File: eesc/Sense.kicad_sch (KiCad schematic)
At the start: 0 parts

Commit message: Add current sense and finish DRV8301 Circuit
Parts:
- added C30, C32, C33: 100n, symbol Device:C
- added IC1, IC2, IC3: MC74VHC1GT66, SOT95P275X110-5N, symbol MC74VHC1GT66:MC74VHC1GT66
- added Q1: DMN62D0U, Package_TO_SOT_SMD_AKL:SOT-23, symbol PCM_Transistor_MOSFET_AKL:DMN62D0U
- added R10, R12, R7, R9: 2.2k, symbol Device:R
- added R11, R13, R6, R8: 39k, symbol Device:R
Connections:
- new net: C33.2, IC3.1 (IN/OUT_XA)
- new net: C30.2, IC1.1 (IN/OUT_XA)
- new net: C32.2, IC2.1 (IN/OUT_XA)
- new net: Q1.3 (D), R6.2
- new net +3.3V: IC1.5 (VCC), IC2.5 (VCC), IC3.5 (VCC)
- new net +5V: Q1.1 (G)
- new net GND: IC1.2 (OUT/IN_YA), IC1.3 (GND), IC2.2 (OUT/IN_YA), IC2.3 (GND), IC3.2 (OUT/IN_YA), IC3.3 (GND), R10.1, R12.1, R7.2, R9.1
- new net SENS_A: C30.1, R8.1, R9.2
- new net SENS_B: C32.1, R10.2, R11.1
- new net SENS_C: C33.1, R12.2, R13.1
- new net SENS_FILTERED: IC1.4 (ON/OFF_CONTROL), IC2.4 (ON/OFF_CONTROL), IC3.4 (ON/OFF_CONTROL)
- new net SENS_SUPPLY: Q1.2 (S), R7.1
- new net SH_A: R8.2
- new net SH_B: R11.2
- new net SH_C: R13.2
- new net V_SUPPLY: R6.1
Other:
- note added: "Current Sensing is implemented to figure out rotor position and apply proper signals to maximimze torque on motor"
- note added: "Current Sensor A"
- note added: "Current Sensor B"
- note added: "Current Sensor C"
- note added: "Power Sense"

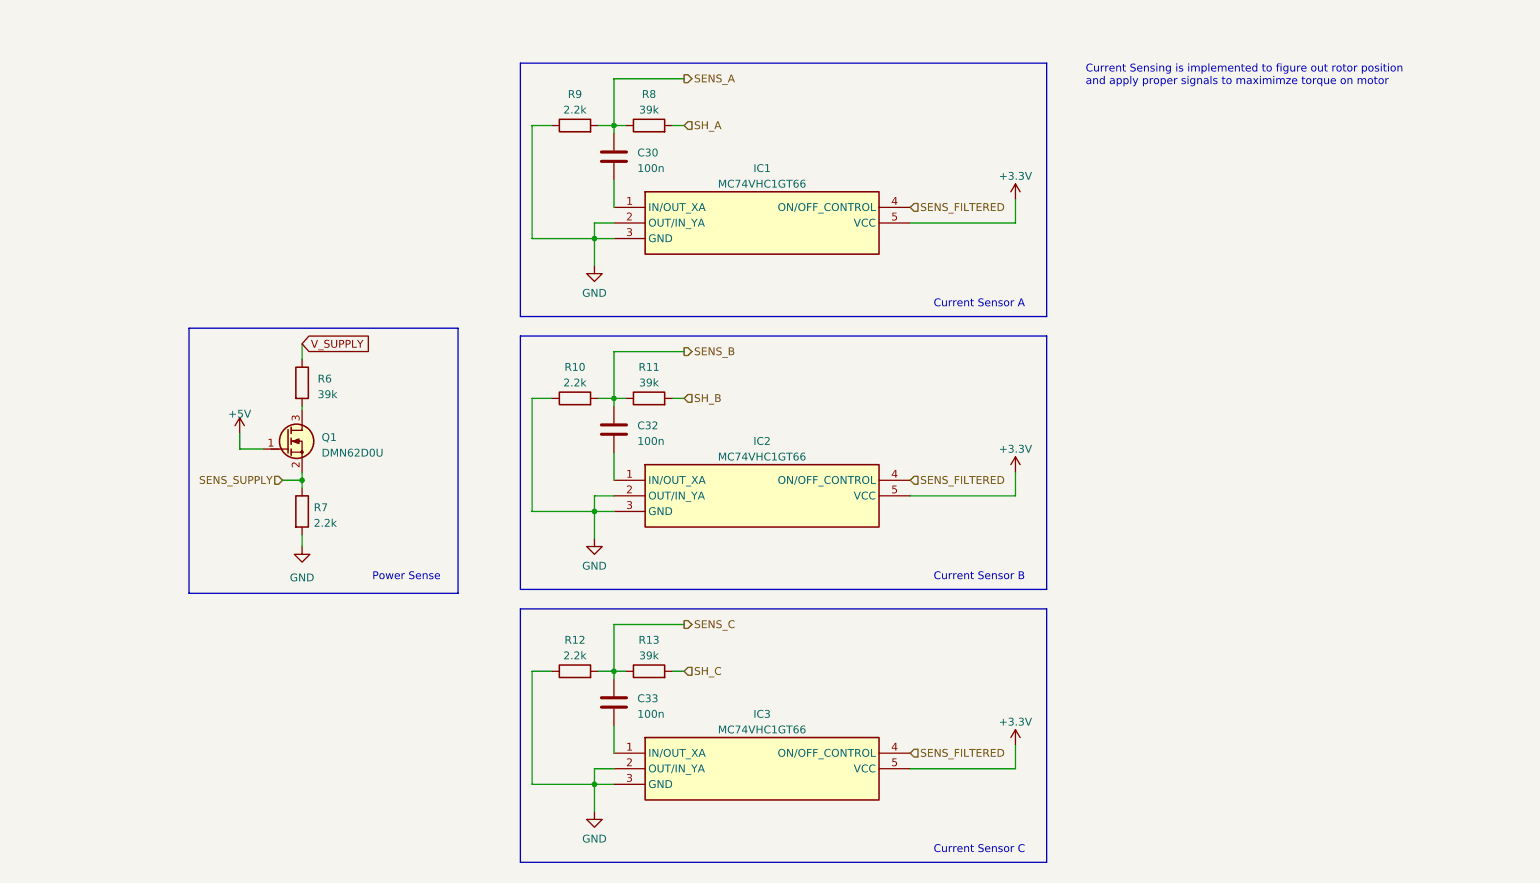
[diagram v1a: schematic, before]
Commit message: Complete transistor stage
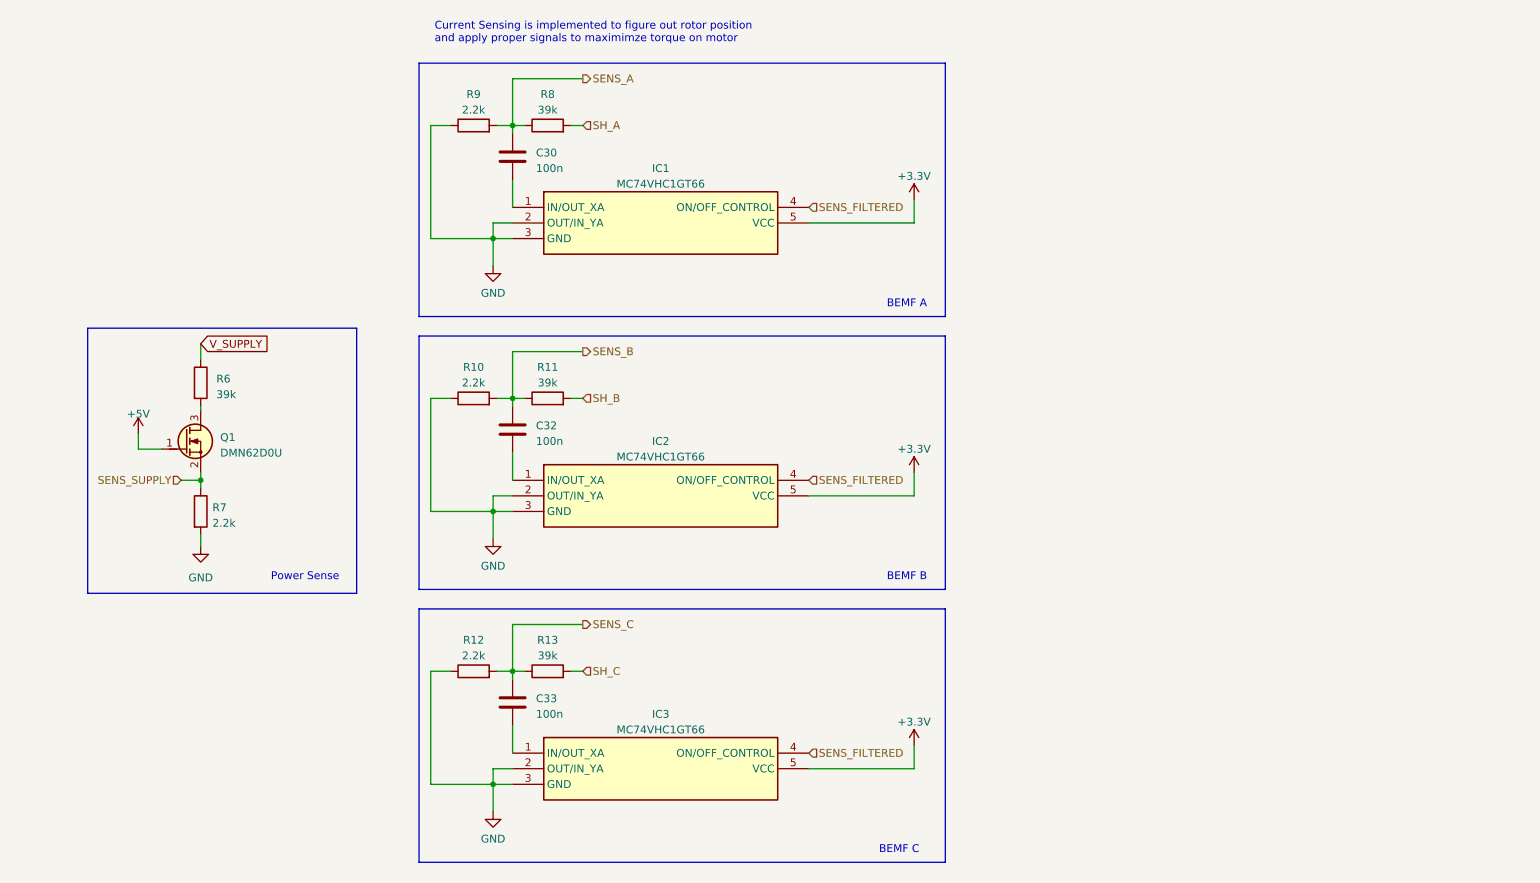
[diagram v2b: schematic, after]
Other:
- note added: "BEMF A"
- note added: "BEMF B"
- note added: "BEMF C"
- note removed: "Current Sensor A"
- note removed: "Current Sensor B"
- note removed: "Current Sensor C"
- moved on the sheet: C30, C32, C33, IC1, IC2, IC3, Q1, R10, R11, R12, R13, R6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

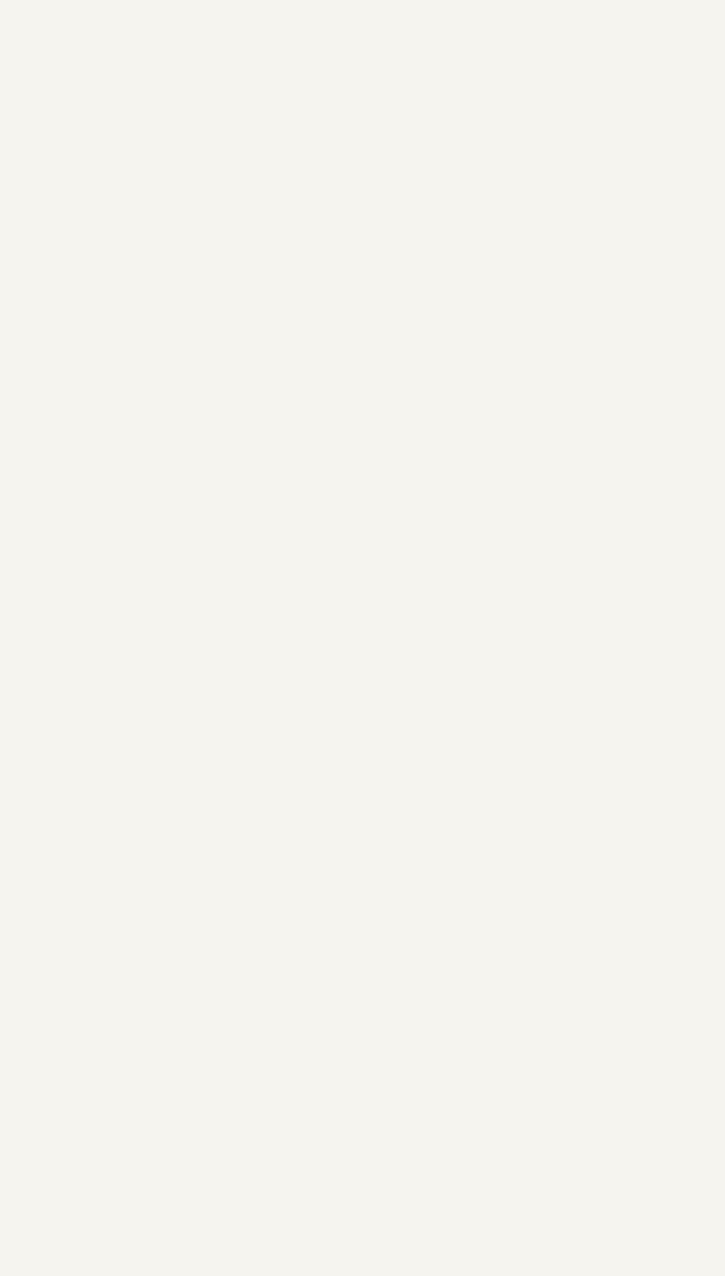
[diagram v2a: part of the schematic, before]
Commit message: Finish current sense
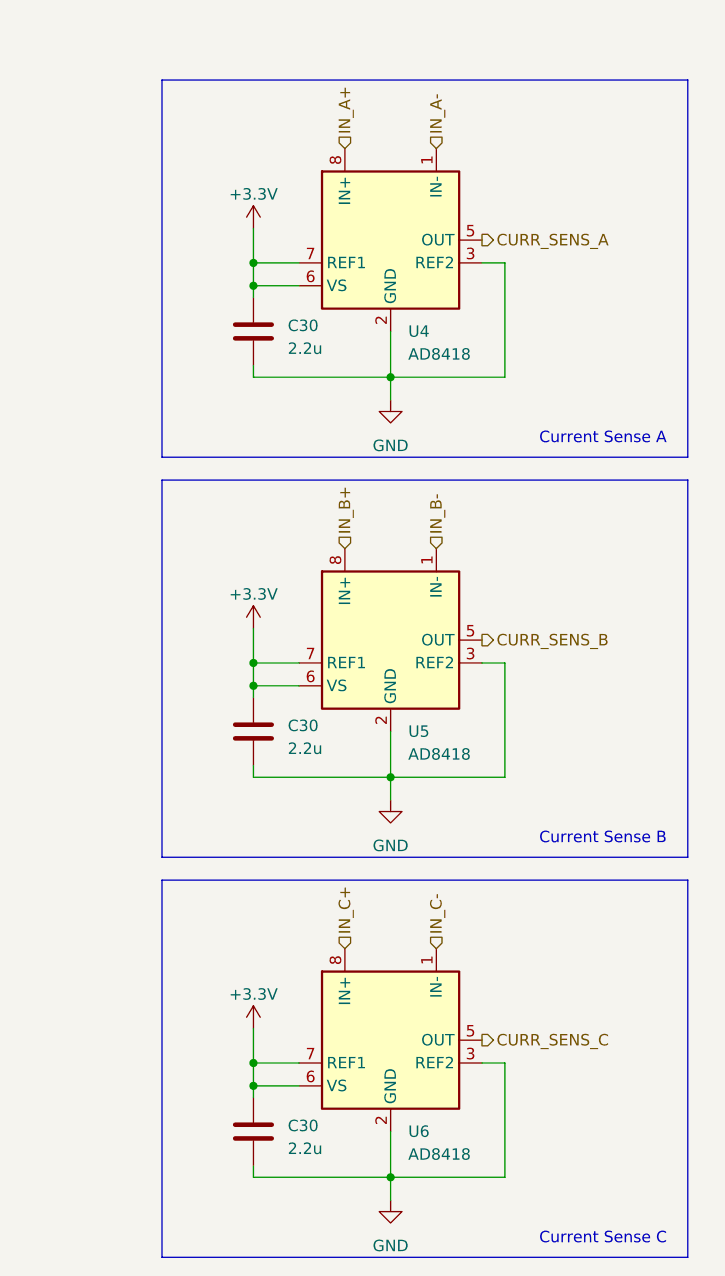
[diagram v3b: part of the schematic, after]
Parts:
- added C30 (x3): 2.2u, symbol Device:C
- added U4, U5, U6: AD8418, symbol Amplifier_Current:AD8418
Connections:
- net +3.3V: now also C30.1, C30.1, C30.1, U4.6 (VS), U4.7 (REF1), U5.6 (VS), U5.7 (REF1), U6.6 (VS), U6.7 (REF1)
- net GND: now also C30.2, C30.2, C30.2, U4.2 (GND), U4.3 (REF2), U5.2 (GND), U5.3 (REF2), U6.2 (GND), U6.3 (REF2)
- new net CURR_SENS_A: U4.5 (OUT)
- new net CURR_SENS_B: U5.5 (OUT)
- new net CURR_SENS_C: U6.5 (OUT)
- new net IN_A+: U4.8 (IN+)
- new net IN_A-: U4.1 (IN-)
- new net IN_B+: U5.8 (IN+)
- new net IN_B-: U5.1 (IN-)
- new net IN_C+: U6.8 (IN+)
- new net IN_C-: U6.1 (IN-)
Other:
- note added: "Current Sense A"
- note added: "Current Sense B"
- note added: "Current Sense C"

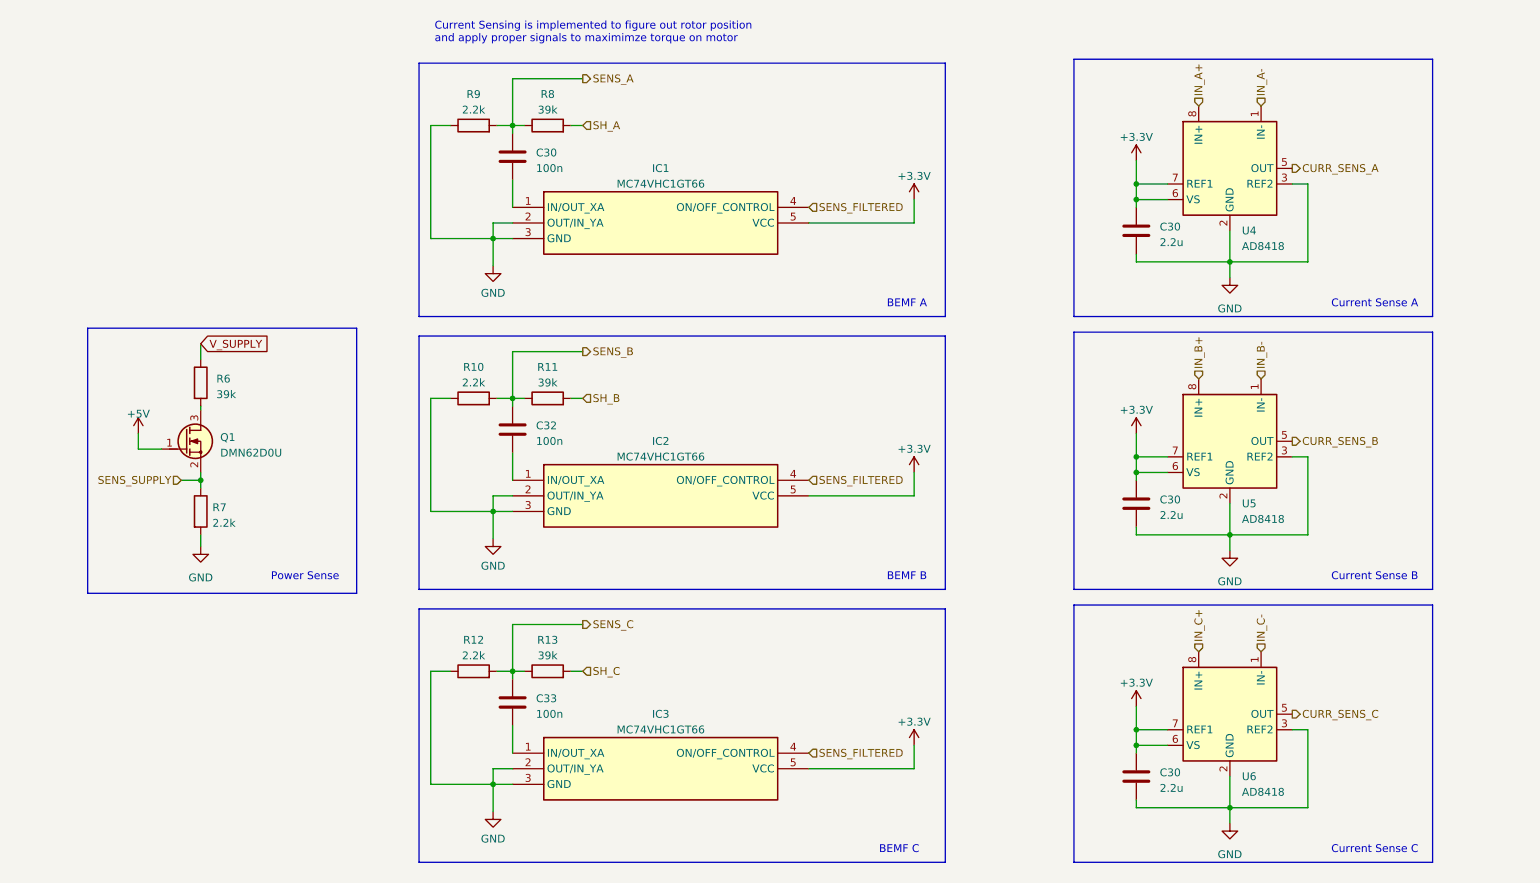
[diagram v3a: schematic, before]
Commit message: Finish up current sense
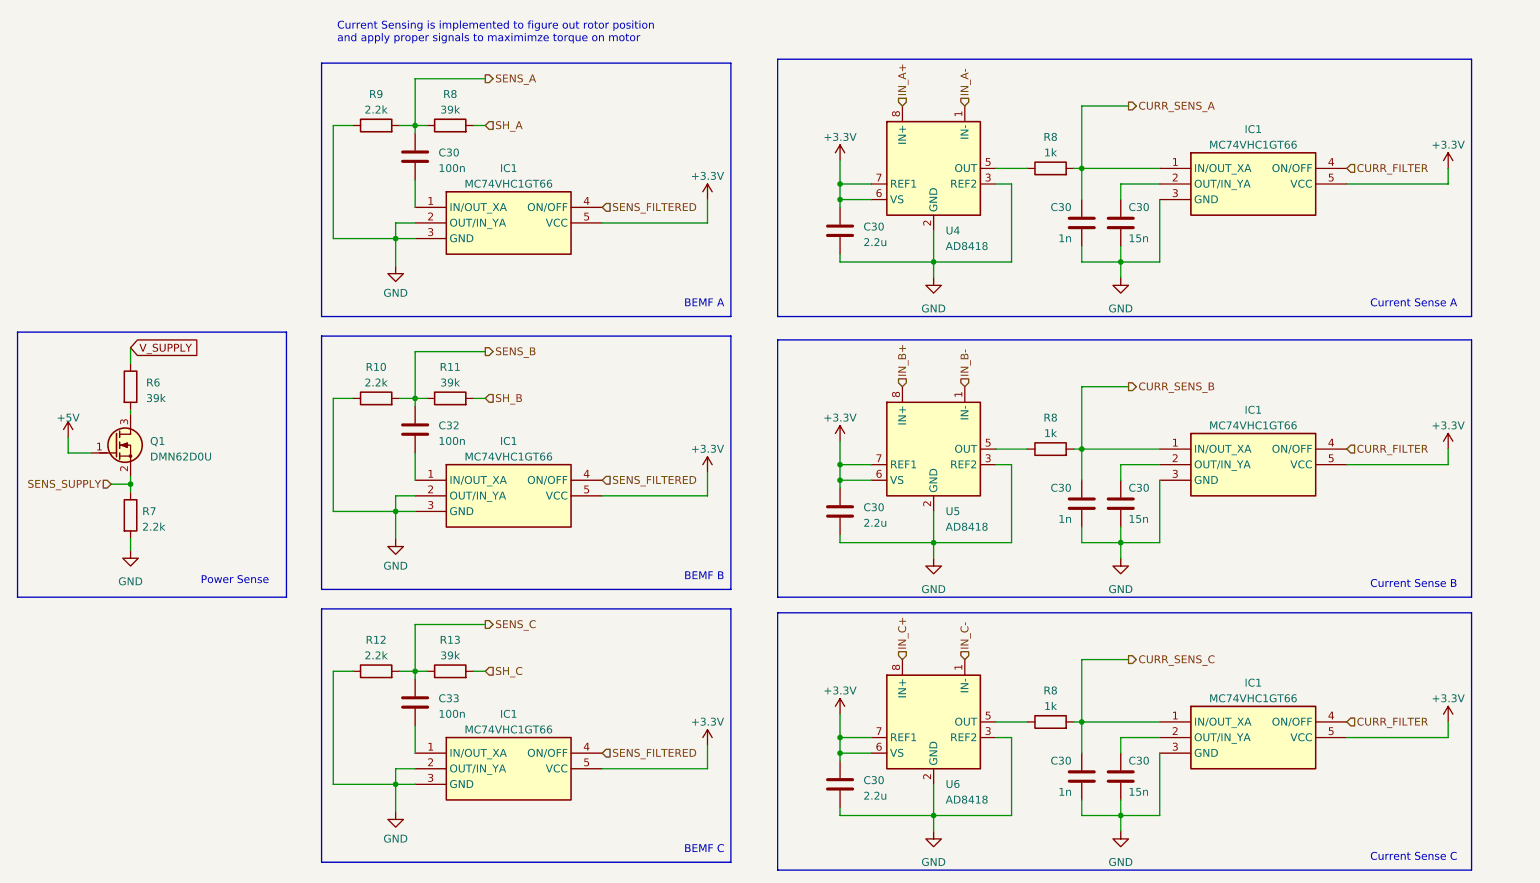
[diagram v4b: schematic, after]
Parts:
- removed C30 (x2): 2.2u, symbol Device:C
- removed IC2, IC3: MC74VHC1GT66, SOT95P275X110-5N, symbol MC74VHC1GT66:MC74VHC1GT66
- added C30 (x2): 2.2u, symbol Device:C
- added C30 (x3): 1n, symbol Device:C
- added C30 (x3): 15n, symbol Device:C
- added IC1 (x5): MC74VHC1GT66, SOT95P275X110-5N, symbol MC74VHC1GT66:MC74VHC1GT66
- added R8 (x3): 1k, symbol Device:R
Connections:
- net +3.3V: now also C30.1, C30.1, IC1.5 (VCC), IC1.5 (VCC), IC1.5 (VCC), IC1.5 (VCC), IC1.5 (VCC)
- net CURR_SENS_A: now also C30.1, IC1.1 (IN/OUT_XA), R8.2; no longer U4.5 (OUT)
- net CURR_SENS_B: now also C30.1, IC1.1 (IN/OUT_XA), R8.2; no longer U5.5 (OUT)
- net CURR_SENS_C: now also C30.1, IC1.1 (IN/OUT_XA), R8.2; no longer U6.5 (OUT)
- net GND: now also C30.2, C30.2, C30.2, C30.2, C30.2, C30.2, C30.2, C30.2, IC1.2 (OUT/IN_YA), IC1.2 (OUT/IN_YA), IC1.3 (GND), IC1.3 (GND), IC1.3 (GND), IC1.3 (GND), IC1.3 (GND)
- net SENS_FILTERED: now also IC1.4 (ON/OFF), IC1.4 (ON/OFF)
- net at C33.2: now also IC1.1 (IN/OUT_XA)
- net at C32.2: now also IC1.1 (IN/OUT_XA)
- new net: R8.1, U5.5 (OUT)
- new net: C30.1, IC1.2 (OUT/IN_YA) (x3)
- new net: R8.1, U6.5 (OUT)
- new net: R8.1, U4.5 (OUT)
- new net CURR_FILTER: IC1.4 (ON/OFF), IC1.4 (ON/OFF), IC1.4 (ON/OFF)
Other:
- moved on the sheet: C30, C32, C33, IC1, Q1, R10, R11, R12, R13, R6, R7, R8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

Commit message: Most updated changes
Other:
- note added: "BEMF Sense"
- note added: "Current Sense"
- note removed: "Current Sensing is implemented to figure out rotor position and apply proper signals to maximimze torque on motor"
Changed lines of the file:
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@@
     (effects (font (size 1.27 1.27)) (justify left bottom))
   )
-  (text "Current Sensing is implemented to figure out rotor position\nand apply proper signals to maximimze torque on motor"
-    (at 73.025 26.67 0)
-    (effects (font (size 1.27 1.27)) (justify left bottom))
+  (text "Current Sense" (at 146.05 26.67 0)
+    (effects (font (size 3 3)) (justify left bottom))
   )
   (text "BEMF A\n" (at 129.54 69.85 0)
     (effects (font (size 1.27 1.27)) (justify left bottom))
   )
+  (text "BEMF Sense" (at 71.12 26.67 0)
+    (effects (font (size 3 3)) (justify left bottom))
+  )
   (text "Current Sense B\n" (at 241.3 115.57 0)
